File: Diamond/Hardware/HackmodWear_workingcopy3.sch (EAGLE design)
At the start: 125 parts, among them Q1 ZXMP6A13F, U1 ATSAMD21G-A, U2 3.3V, U5 OPA344, U6 ADMP401, U7 APDS-9960, Y1 32.768kHz

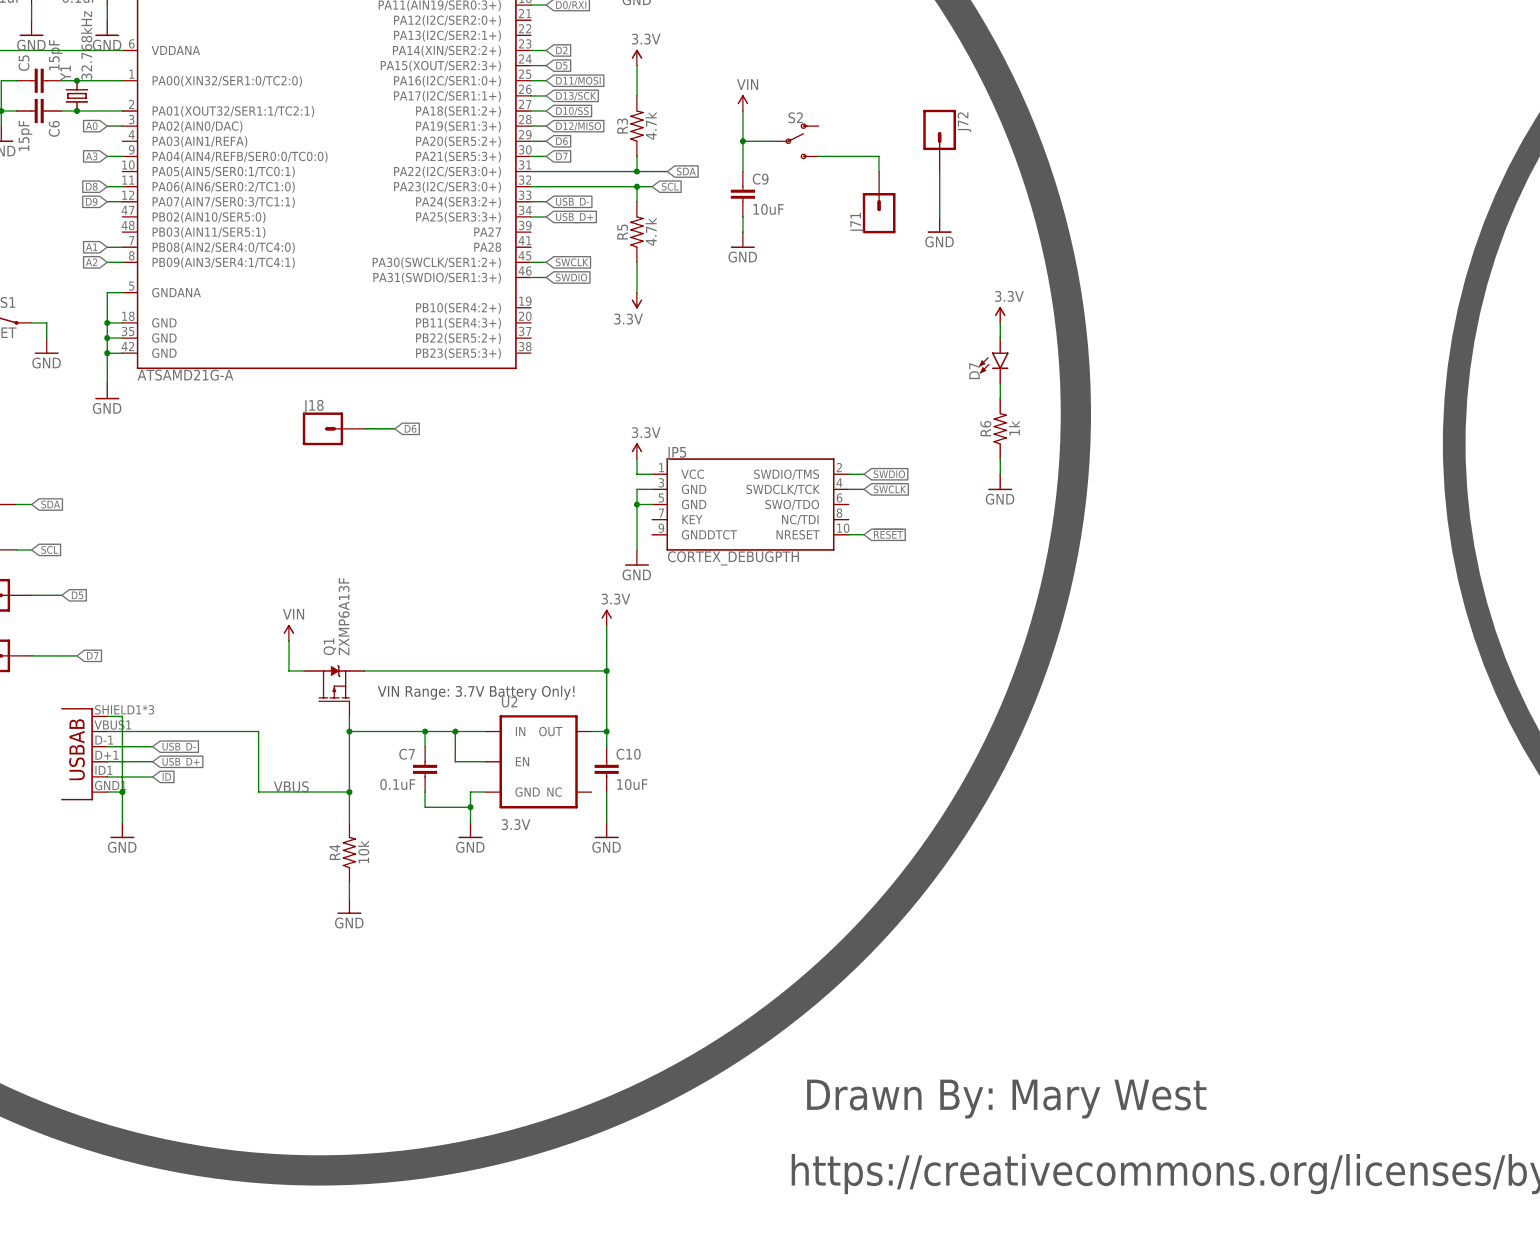
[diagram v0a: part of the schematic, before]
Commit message: Updates to power supply section
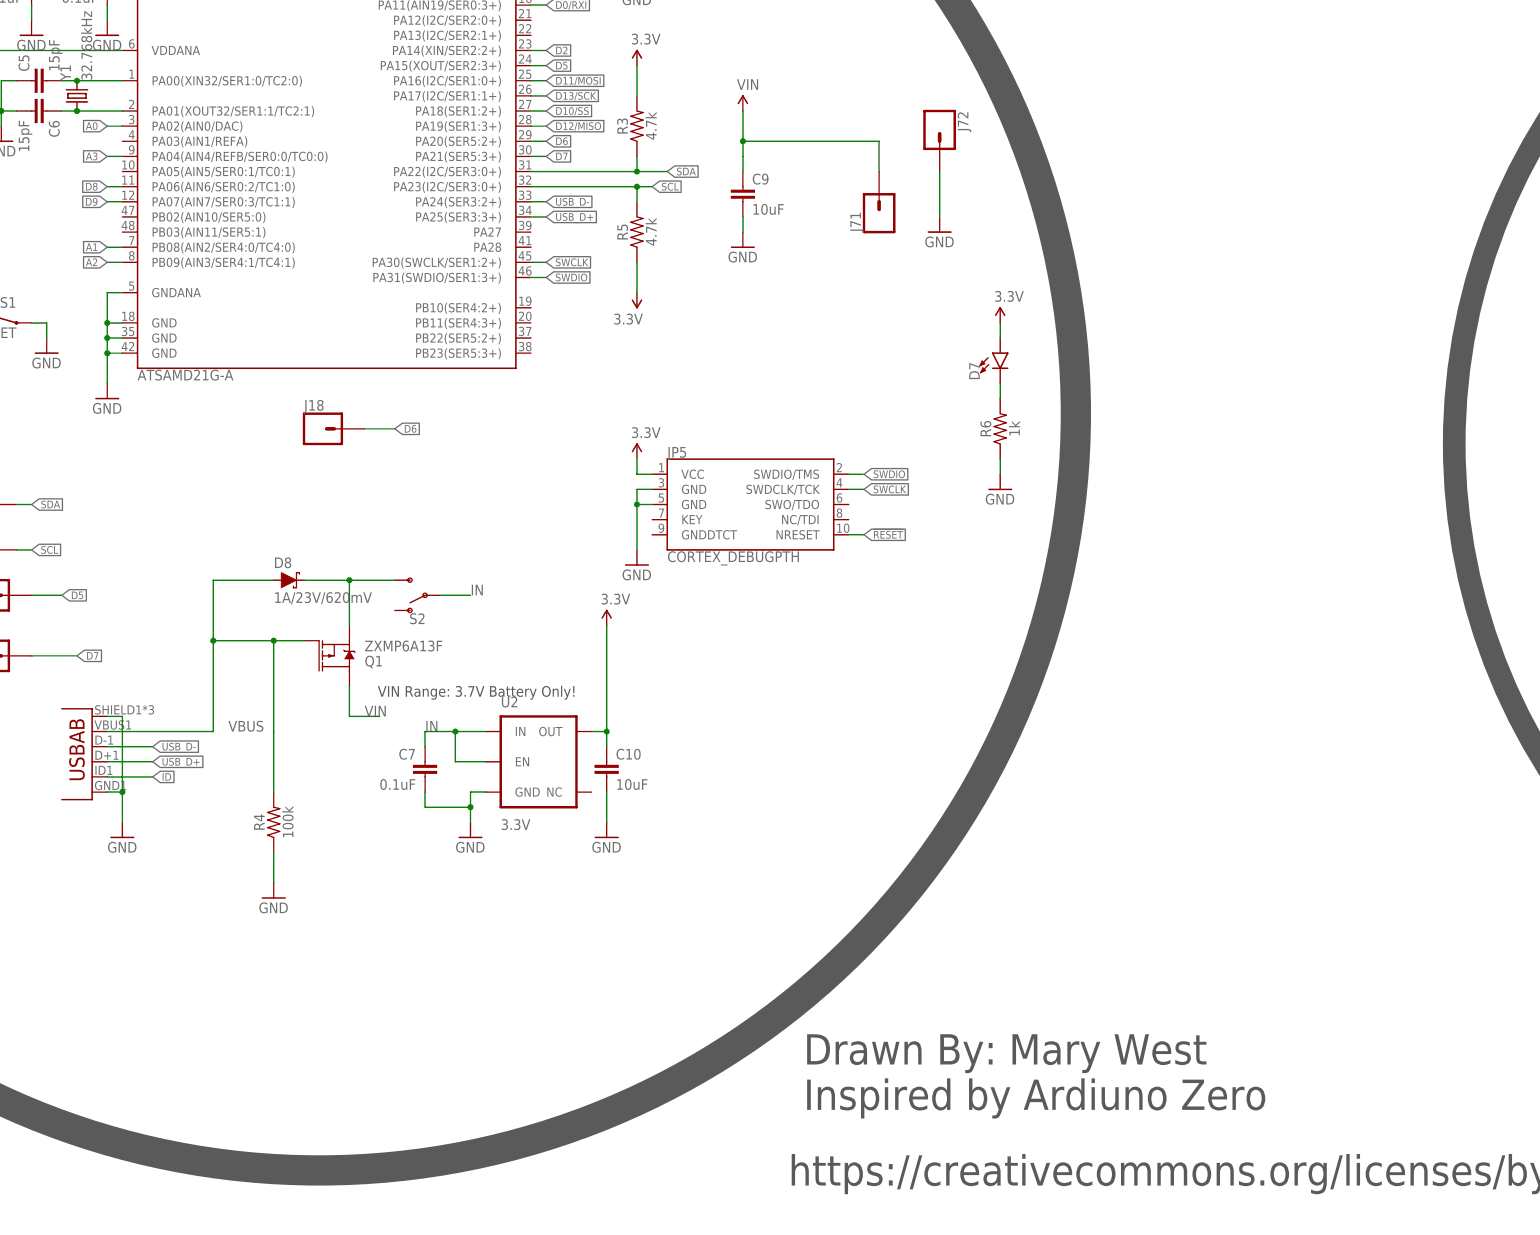
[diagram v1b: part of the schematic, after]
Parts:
- added D8: 1A/23V/620mV, SparkFun-DiscreteSemi:DIODE-SCHOTTKY-BAT20J
- R4: value 10k -> 100k; device SparkFun-Resistors:10KOHM-0603-1/10W-1% -> SparkFun-Resistors:100KOHM-0603-1/10W-1%
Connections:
- removed net N$21: J71.1, S2.S
- new net IN: C7.1, S2.P, U2.EN, U2.IN
- new net N$8: D8.C, Q1.S, S2.S
- net 3.3V: no longer Q1.S
- net VBUS: now also D8.A; no longer C7.1, U2.EN, U2.IN
- net VIN: now also J71.1; no longer S2.P
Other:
- note added: "Drawn By: Mary West Inspired by Ardiuno Zero"
- note removed: "Drawn By: Mary West"
- moved on the sheet: Q1, R4, S2
